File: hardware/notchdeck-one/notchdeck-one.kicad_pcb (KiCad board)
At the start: 4 copper layers, 145 x 105 mm, 144 parts, among them J1 USB-C, J10 POWER MAG, J11 BRAKE MAG, J12 POWER GRAY, J2 BAT 1S, J3 SWD, J4 TC2030_NL, J5 BRAKE / MASCON GRAY, J9 REV F-N-R, Q1 AO3401A, SW1 SW_Push, SW10 SW_Push, SW11 SW_Push, SW12 SW_Push, SW13 SW_Push, SW14 SW_Push, SW15 SW_Push, SW16 SW_Push, SW17 RESET, SW2 SW_Push, SW3 SW_Push, SW4 SW_Push, SW5 SW_Push, SW6 SW_Push, SW7 SW_Push, SW8 SW_Push, SW9 SW_Push, U1 E73-2G4M08S1C, U10 USBLC6-2SC6, U11 USBLC6-2SC6, U2 AP2112K-3.3, U3 MCP73832-2-OT, U4 MAX17048, U5 AS5600, U7 USBLC6-2SC6, U8 74AHCT1G125, U9 TCA9543APWR

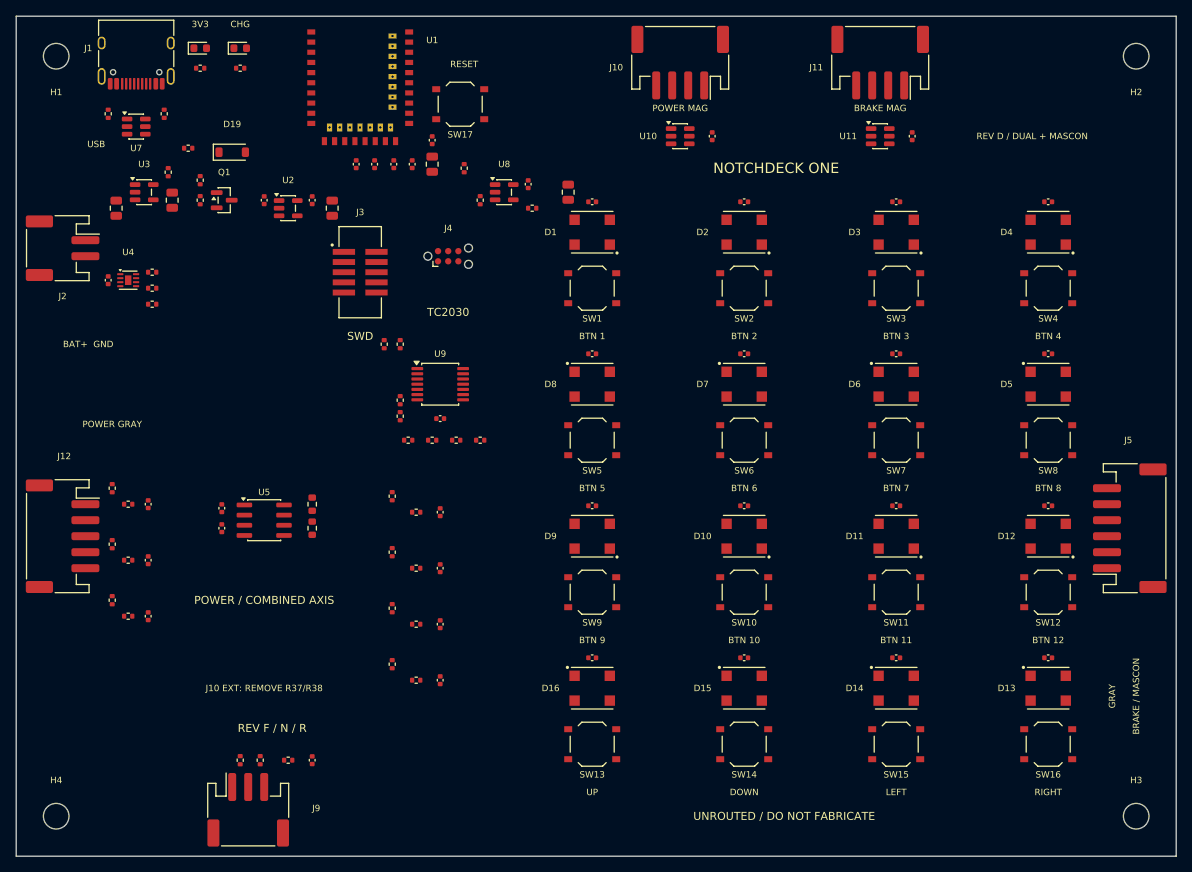
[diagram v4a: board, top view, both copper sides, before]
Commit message: Split controller buttons onto stocked STM32G030 panel PCB
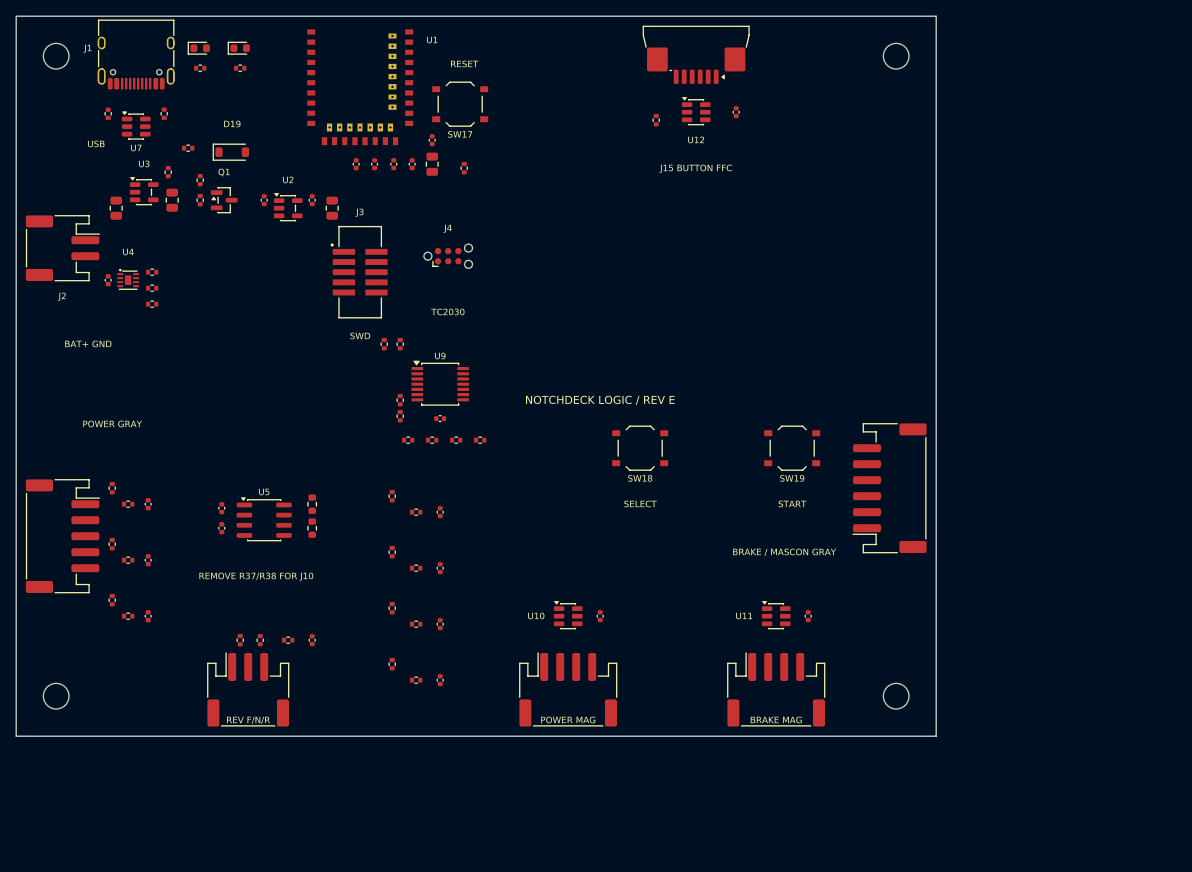
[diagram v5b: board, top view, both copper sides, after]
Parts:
- removed C13: 1uF, Capacitor_SMD:C_0805_2012Metric
- removed C20, C21, C22, C23, C24, C25, C26, C27, C28, C29, C30, C31, C32, C33, C34, C35, C36: 100nF, Capacitor_SMD:C_0402_1005Metric
- removed D1, D10, D11, D12, D13, D14, D15, D16, D2, D3, D4, D5, D6, D7, D8, D9: WS2812B, notchdeck:LED_XINGLIGHT_XL-5050RGBC-2812B
- removed R11: 330, Resistor_SMD:R_0402_1005Metric
- removed R26: 100k, Resistor_SMD:R_0402_1005Metric
- removed SW1, SW10, SW11, SW12, SW13, SW14, SW15, SW16, SW2, SW3, SW4, SW5, SW6, SW7, SW8, SW9: SW_Push, Button_Switch_SMD:SW_Push_1P1T_XKB_TS-1187A
- removed U8: 74AHCT1G125, Package_TO_SOT_SMD:SOT-23-5
- added C44: 100nF, Capacitor_SMD:C_0402_1005Metric, F.Cu at (140.0, 62.0)
- added J15: BUTTON MCU FFC, Connector_FFC-FPC:JUSHUO_AFA07-S06FCA-00_1x6-1MP_P1.0mm_Horizontal, F.Cu at (135.0, 54.2)
- added R42: 10k, Resistor_SMD:R_0402_1005Metric, F.Cu at (130.0, 63.0)
- added SW18: SELECT, Button_Switch_SMD:SW_Push_1P1T_XKB_TS-1187A, F.Cu at (128.0, 104.0)
- added SW19: START, Button_Switch_SMD:SW_Push_1P1T_XKB_TS-1187A, F.Cu at (147.0, 104.0)
- added U12: USBLC6-2SC6, Package_TO_SOT_SMD:SOT-23-6, F.Cu at (135.0, 62.0)
- moved J10 79.6 mm to (119.0, 134.2), turned to 0 degrees
- moved J11 79.5 mm to (145.0, 134.2), turned to 0 degrees
- moved C39 61.6 mm to (123.0, 125.0)
- moved U10 61.6 mm to (119.0, 125.0)
- moved C40 61.4 mm to (149.0, 125.0)
- moved U11 61.4 mm to (145.0, 125.0)
- moved H3 33.5 mm to (160.0, 135.0)
- moved J5 30.4 mm to (159.2, 109.0)
- moved H2 30.0 mm to (160.0, 55.0)
- moved J9 15.0 mm to (79.0, 134.2)
- moved C37 15.0 mm to (87.0, 128.0)
- moved H4 15.0 mm to (55.0, 135.0)
- moved R23 15.0 mm to (78.0, 128.0)
- moved R24 15.0 mm to (80.5, 128.0)
- moved R25 15.0 mm to (84.0, 128.0)
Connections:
- U1 pad 1: /BTN1 -> /PANEL_INT
- U1 pad 11: /BTN11 -> unconnected-(U1-P0.00/XL1-Pad11)
- U1 pad 13: /BTN12 -> unconnected-(U1-P0.01/XL2-Pad13)
- U1 pad 16: /WS2812_DIN -> unconnected-(U1-P0.08-Pad16)
- U1 pad 17: /BTN4 -> unconnected-(U1-P1.09-Pad17)
- U1 pad 2: /BTN2 -> unconnected-(U1-P1.10-Pad2)
- U1 pad 32: /BTN5 -> unconnected-(U1-P0.20-Pad32)
- U1 pad 33: /BTN6 -> unconnected-(U1-P0.13-Pad33)
- U1 pad 34: /HAT_UP -> unconnected-(U1-P0.22-Pad34)
- U1 pad 35: /HAT_DOWN -> unconnected-(U1-P0.24-Pad35)
- U1 pad 36: /HAT_LEFT -> unconnected-(U1-P1.00-Pad36)
- U1 pad 38: /HAT_RIGHT -> unconnected-(U1-P1.02-Pad38)
- U1 pad 41: /BTN9 -> unconnected-(U1-P0.09/NFC1-Pad41)
- U1 pad 43: /BTN10 -> unconnected-(U1-P0.10/NFC2-Pad43)
- U1 pad 6: /BTN3 -> unconnected-(U1-P1.13-Pad6)
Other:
- board size 145 x 105 mm -> 115 x 90 mm
- board text added: "BRAKE / MASCON GRAY"
- board text added: "J12: 1 GND / 2..4 POWER S0..S2 / 5 3V3"
- board text added: "J15 -> BUTTON J1: 6-WAY 1mm FFC TYPE A"
- board text added: "J15 BUTTON FFC"
- board text added: "J15: 1 GND / 2 3V3 / 3 SDA / 4 SCL / 5 IRQ / 6 USB5V"
- board text added: "J5: 1 GND / 2..5 BRAKE S0..S3 / 6 3V3"
- board text added: "MAIN PIN n -> BUTTON PIN 7-n - POWER OFF TO INSERT"
- board text added: "NOTCHDECK LOGIC / REV E"
- board text added: "PASSIVE GRAY CAMS: LEAVE 3V3 CAVITY EMPTY"
- board text added: "PROVISIONAL 115 x 90 mm / UNROUTED - DO NOT FABRICATE"
- board text added: "REMOVE R37/R38 FOR J10"
- board text added: "REV F/N/R"
- board text added: "SELECT"
- board text added: "START"
- board text added: "SW18 SELECT=BTN7; SW19 START=BTN8 (PARALLEL)"
- board text removed: "3V3"
- board text removed: "Align magnet to U5 center"
- board text removed: "BRAKE / MASCON"
- board text removed: "BTN 1"
- board text removed: "BTN 10"
- board text removed: "BTN 11"
- board text removed: "BTN 12"
- board text removed: "BTN 2"
- board text removed: "BTN 3"
- board text removed: "BTN 4"
- board text removed: "BTN 5"
- board text removed: "BTN 6"
- board text removed: "BTN 7"
- board text removed: "BTN 8"
- board text removed: "BTN 9"
- board text removed: "CHG"
- board text removed: "DOWN"
- board text removed: "GRAY"
- board text removed: "GRAY CONTACTS: LEAVE 3V3 WIRE OUT"
- board text removed: "J10 EXT: REMOVE R37/R38"
- board text removed: "J12 POWER: 1 GND / 2 S0 / 3 S1 / 4 S2 / 5 3V3"
- board text removed: "J5 BRAKE / MASCON: 1 GND / 2 S0 / 3 S1 / 4 S2 / 5 S3 / 6 3V3"
- board text removed: "LEFT"
- board text removed: "NOTCHDECK ONE"
- board text removed: "POWER / COMBINED AXIS"
- board text removed: "PROVISIONAL 145 x 105 mm - MECHANICS TBD"
- board text removed: "REV D / DUAL + MASCON"
- board text removed: "REV F / N / R"
- board text removed: "RIGHT"
- board text removed: "UNROUTED / DO NOT FABRICATE"
- board text removed: "UP"

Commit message: Add protected PWM actuator outputs and charger interlock
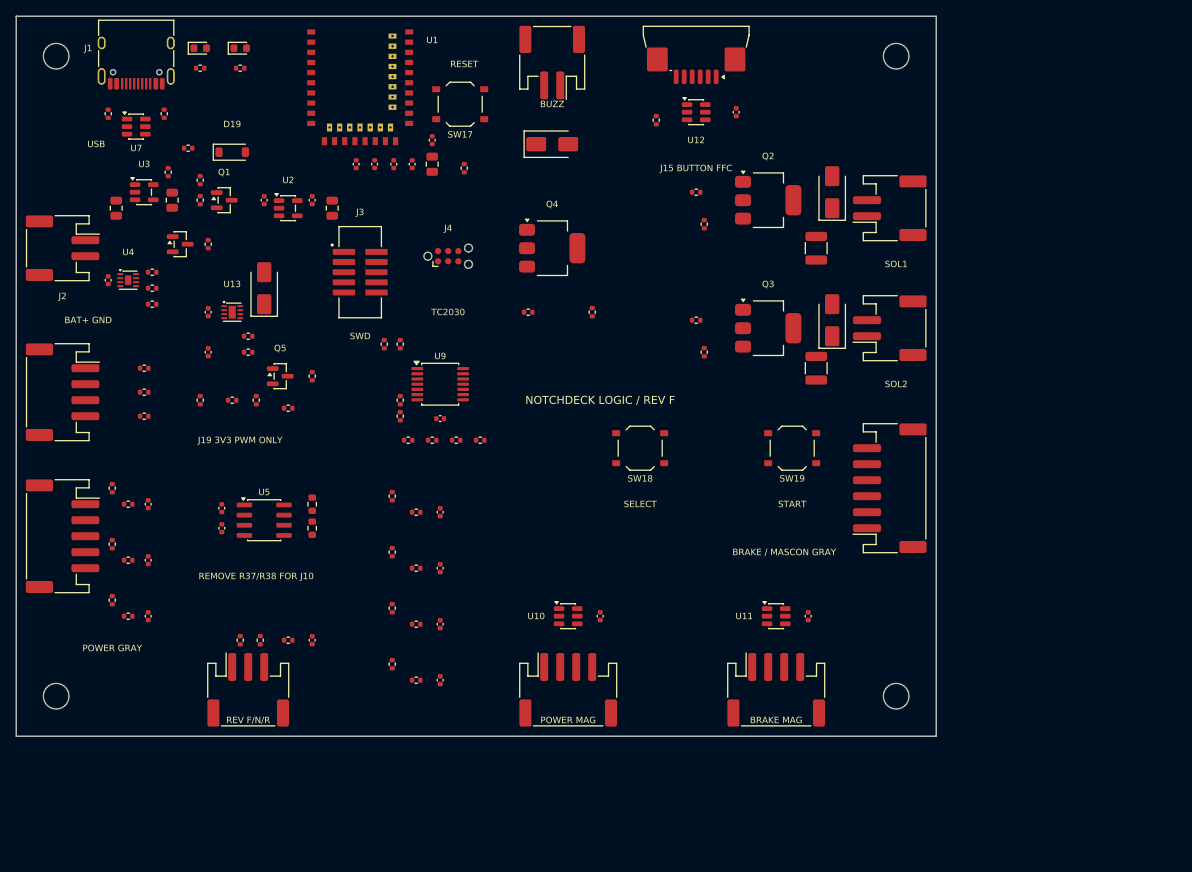
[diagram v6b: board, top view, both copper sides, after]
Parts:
- added C45: 22uF, Capacitor_SMD:C_1210_3225Metric, F.Cu at (150.0, 79.0)
- added C46: 22uF, Capacitor_SMD:C_1210_3225Metric, F.Cu at (150.0, 94.0)
- added C47: 1uF, Capacitor_SMD:C_0402_1005Metric, F.Cu at (74.0, 87.0)
- added C48: 100nF, Capacitor_SMD:C_0402_1005Metric, F.Cu at (74.0, 92.0)
- added D20: B360A, Diode_SMD:D_SMA, F.Cu at (152.0, 72.0)
- added D21: B360A, Diode_SMD:D_SMA, F.Cu at (152.0, 88.0)
- added D22: B360A, Diode_SMD:D_SMA, F.Cu at (117.0, 66.0)
- added D23: B360A, Diode_SMD:D_SMA, F.Cu at (81.0, 84.0)
- added J16: SOLENOID 1, Connector_JST:JST_PH_S2B-PH-SM4-TB_1x02-1MP_P2.00mm_Horizontal, F.Cu at (159.2, 74.0)
- added J17: SOLENOID 2, Connector_JST:JST_PH_S2B-PH-SM4-TB_1x02-1MP_P2.00mm_Horizontal, F.Cu at (159.2, 89.0)
- added J18: ACTIVE BUZZER, Connector_JST:JST_PH_S2B-PH-SM4-TB_1x02-1MP_P2.00mm_Horizontal, F.Cu at (117.0, 55.8)
- added J19: EXTERNAL PWM 3V3, Connector_JST:JST_PH_S4B-PH-SM4-TB_1x04-1MP_P2.00mm_Horizontal, F.Cu at (55.8, 97.0)
- added Q2: ZXMS6005DGTA, Package_TO_SOT_SMD:SOT-223-3_TabPin2, F.Cu at (144.0, 73.0)
- added Q3: ZXMS6005DGTA, Package_TO_SOT_SMD:SOT-223-3_TabPin2, F.Cu at (144.0, 89.0)
- added Q4: ZXMS6005DGTA, Package_TO_SOT_SMD:SOT-223-3_TabPin2, F.Cu at (117.0, 79.0)
- added Q5: 2N7002, Package_TO_SOT_SMD:SOT-23, F.Cu at (83.0, 95.0)
- added Q6: 2N7002, Package_TO_SOT_SMD:SOT-23, F.Cu at (70.5, 78.5)
- added R43: 330, Resistor_SMD:R_0402_1005Metric, F.Cu at (135.0, 72.0)
- added R44: 330, Resistor_SMD:R_0402_1005Metric, F.Cu at (135.0, 88.0)
- added R45: 330, Resistor_SMD:R_0402_1005Metric, F.Cu at (114.0, 87.0)
- added R46: 100k, Resistor_SMD:R_0402_1005Metric, F.Cu at (136.0, 76.0)
- added R47: 100k, Resistor_SMD:R_0402_1005Metric, F.Cu at (136.0, 92.0)
- added R48: 100k, Resistor_SMD:R_0402_1005Metric, F.Cu at (122.0, 87.0)
- added R49: 1k, Resistor_SMD:R_0402_1005Metric, F.Cu at (66.0, 94.0)
- added R50: 1k, Resistor_SMD:R_0402_1005Metric, F.Cu at (66.0, 97.0)
- added R51: 1k, Resistor_SMD:R_0402_1005Metric, F.Cu at (66.0, 100.0)
- added R52: 1k, Resistor_SMD:R_0402_1005Metric, F.Cu at (77.0, 98.0)
- added R53: 100k, Resistor_SMD:R_0402_1005Metric, F.Cu at (80.0, 98.0)
- added R54: 1k, Resistor_SMD:R_0402_1005Metric, F.Cu at (84.0, 99.0)
- added R55: 100k, Resistor_SMD:R_0402_1005Metric, F.Cu at (87.0, 95.0)
- added R56: 1k, Resistor_SMD:R_0402_1005Metric, F.Cu at (79.0, 90.0)
- added R57: 10k, Resistor_SMD:R_0402_1005Metric, F.Cu at (73.0, 98.0)
- added R58: 330, Resistor_SMD:R_0402_1005Metric, F.Cu at (79.0, 92.0)
- added R59: 100k, Resistor_SMD:R_0402_1005Metric, F.Cu at (74.0, 78.5)
- added U13: TPS259531DSGR, Package_DFN_QFN:DFN-8-1EP_2x2mm_P0.5mm_EP0.9x1.6mm, F.Cu at (77.0, 87.0)
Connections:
- net /Power/BAT+ renamed /BAT_RAW
- R3 pad 2: GND -> Net-(Q6-D)
- U1 pad 32: unconnected-(U1-P0.20-Pad32) -> /SOL1_PWM
- U1 pad 33: unconnected-(U1-P0.13-Pad33) -> /SOL2_PWM
- U1 pad 34: unconnected-(U1-P0.22-Pad34) -> /BUZZ_PWM
- U1 pad 35: unconnected-(U1-P0.24-Pad35) -> /ACT_EN
- U1 pad 36: unconnected-(U1-P1.00-Pad36) -> /ACT_nFAULT
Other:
- board text added: "BUZZ"
- board text added: "J19 3V3 PWM ONLY"
- board text added: "NOTCHDECK LOGIC / REV F"
- board text added: "SOL1"
- board text added: "SOL2"
- board text removed: "NOTCHDECK LOGIC / REV E"

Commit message: Protect full battery input and size dual 2A impulse outputs
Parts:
- added D24: B360A, Diode_SMD:D_SMA, F.Cu at (87.0, 88.0)
- added R60: 100, Resistor_SMD:R_0603_1608Metric, F.Cu at (74.0, 94.5)
- J2: value BAT 1S -> BAT 1S / 2+2; footprint Connector_JST:JST_PH_S2B-PH-SM4-TB_1x02-1MP_P2.00mm_Horizontal -> Connector_Molex:Molex_Micro-Fit_3.0_43045-0400_2x02_P3.00mm_Horizontal
- R52: value 1k -> 100k
- R56: value 1k -> 330
- U13: value TPS259531DSGR -> TPS259461LRPWR; footprint Package_DFN_QFN:DFN-8-1EP_2x2mm_P0.5mm_EP0.9x1.6mm -> notchdeck:TI_RPW0010A
- moved C10 5.00 mm to (65.5, 86.0)
- moved U4 5.00 mm to (68.0, 86.0)
- moved C19 4.72 mm to (66.5, 76.5)
- moved R6 4.47 mm to (71.0, 84.0)
- moved R7 4.47 mm to (71.0, 86.0)
- moved R8 4.47 mm to (71.0, 88.0)
- moved J2 4.20 mm to (60.0, 79.0), turned to 90 degrees
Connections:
- C10 pad 1: /BAT_RAW -> /BAT_PROT
- C19 pad 1: /BAT_RAW -> /BAT_PROT
- C45 pad 1: /Actuators/ACT_BAT -> /BAT_PROT
- C46 pad 1: /Actuators/ACT_BAT -> /BAT_PROT
- C47 pad 1: /BAT_RAW -> /Actuators/BAT_RAW
- C48 pad 1: Net-(U13-dVdt) -> Net-(C48-Pad1)
- D20 pad 1: /Actuators/ACT_BAT -> /BAT_PROT
- D21 pad 1: /Actuators/ACT_BAT -> /BAT_PROT
- D22 pad 1: /Actuators/ACT_BAT -> /BAT_PROT
- D23 pad 1: /Actuators/ACT_BAT -> /BAT_PROT
- J16 pad 1: /Actuators/ACT_BAT -> /BAT_PROT
- J17 pad 1: /Actuators/ACT_BAT -> /BAT_PROT
- J18 pad 1: /Actuators/ACT_BAT -> /BAT_PROT
- J2 pad 1: /BAT_RAW -> /Actuators/BAT_RAW
- J2 pad 2: GND -> /Actuators/BAT_RAW
- Q1 pad 3: /BAT_RAW -> /BAT_PROT
- R52 pad 1: /ACT_EN -> /Actuators/BAT_RAW
- R52 pad 2: /Actuators/ACT_ENABLE -> /Actuators/BAT_ENABLE
- R53 pad 1: /Actuators/ACT_ENABLE -> /Actuators/BAT_ENABLE
- R57 pad 2: /ACT_nFAULT -> /BAT_nFAULT
- U1 pad 36: /ACT_nFAULT -> /BAT_nFAULT
- U13 pad 1: Net-(U13-dVdt) -> /Actuators/BAT_ENABLE
- U13 pad 2: /Actuators/ACT_ENABLE -> GND
- U13 pad 3: /BAT_RAW -> unconnected-(U13-SPLYGD-Pad3)
- U13 pad 4: /BAT_RAW -> /BAT_nFAULT
- U13 pad 5: /Actuators/ACT_BAT -> /Actuators/BAT_RAW
- U13 pad 6: /ACT_nFAULT -> /BAT_PROT
- U13 pad 7: Net-(U13-ILM) -> Net-(U13-dVdt)
- U13 pad 9: GND -> Net-(U13-ILM)
- U3 pad 3: /BAT_RAW -> /BAT_PROT
- U4 pad 2: /BAT_RAW -> /BAT_PROT
- U4 pad 3: /BAT_RAW -> /BAT_PROT
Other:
- board text added: "J2: 1,2 BAT+ / 3,4 GND"
- board text added: "NOTCHDECK LOGIC / REV G"
- board text removed: "BAT+ GND"
- board text removed: "NOTCHDECK LOGIC / REV F"
